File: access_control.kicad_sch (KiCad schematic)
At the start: 32 parts, among them J1 Conn_01x04_Pin, J2 Screw_Terminal_01x04, J3 Screw_Terminal_01x04, SW1 Reset button, U1 STM32F446RETx, U2 DS3231M, U3 MAX3232ESE, Y1 16MHz

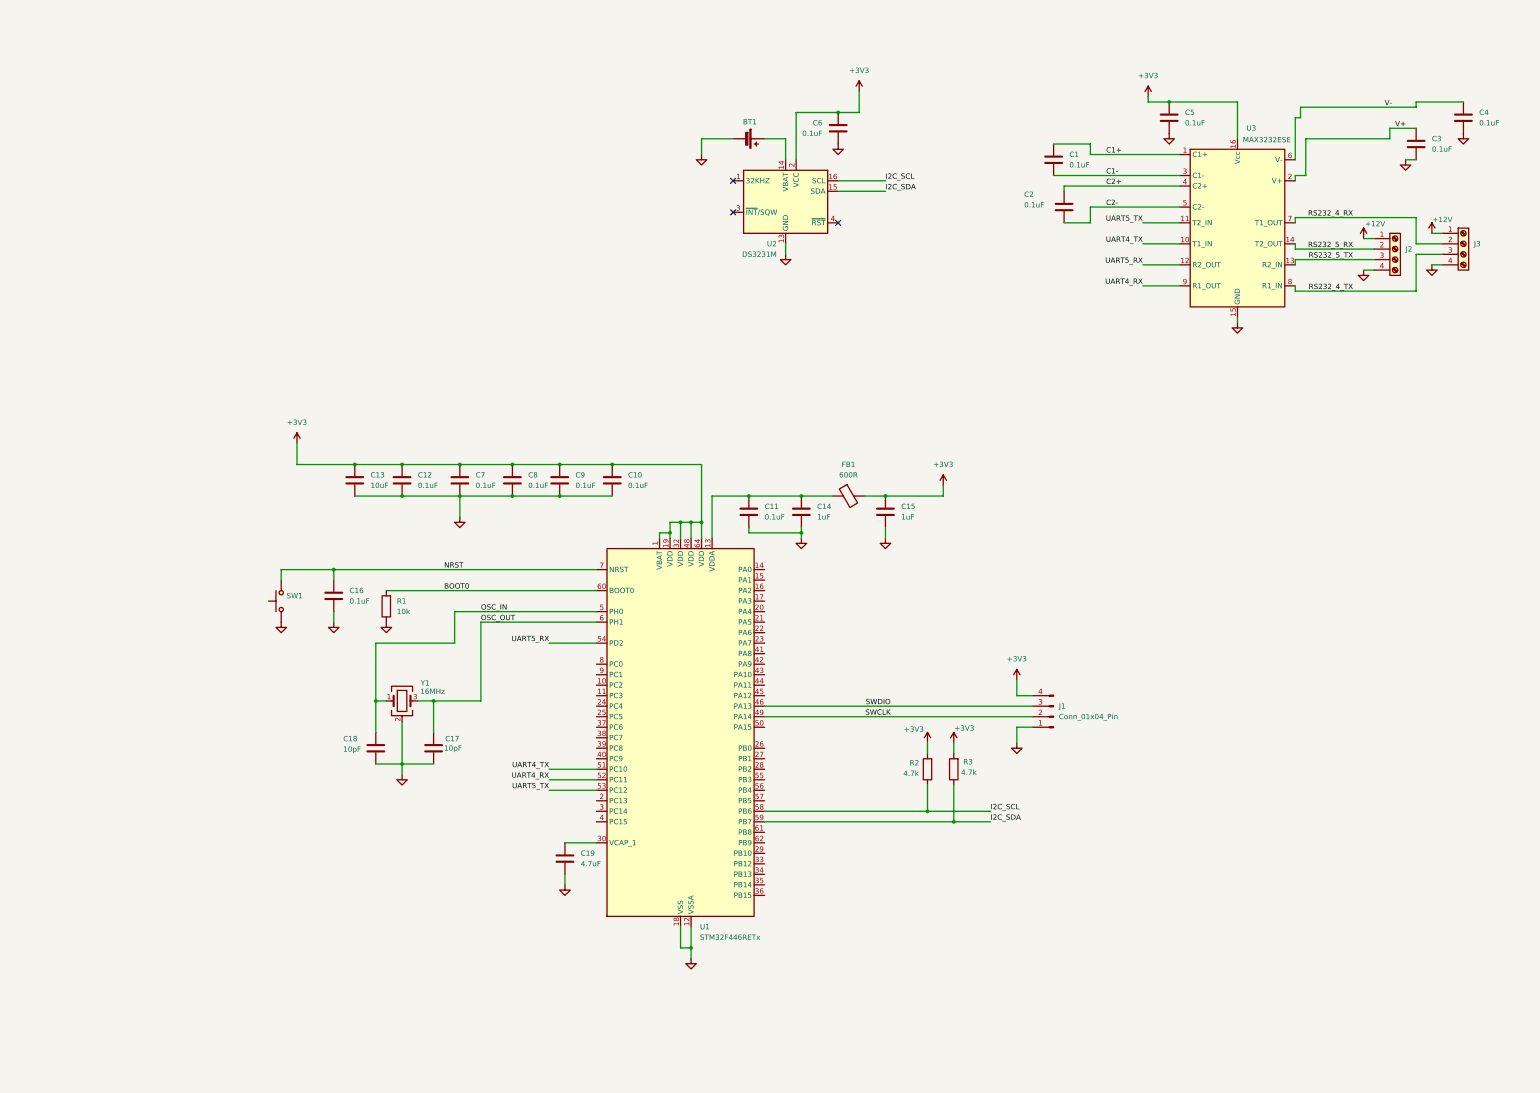
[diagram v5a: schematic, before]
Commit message: Connected the MOSFETS to the door control pins. Added footprints and info about the mosfets that i will use. Same information added for the voltage regulator
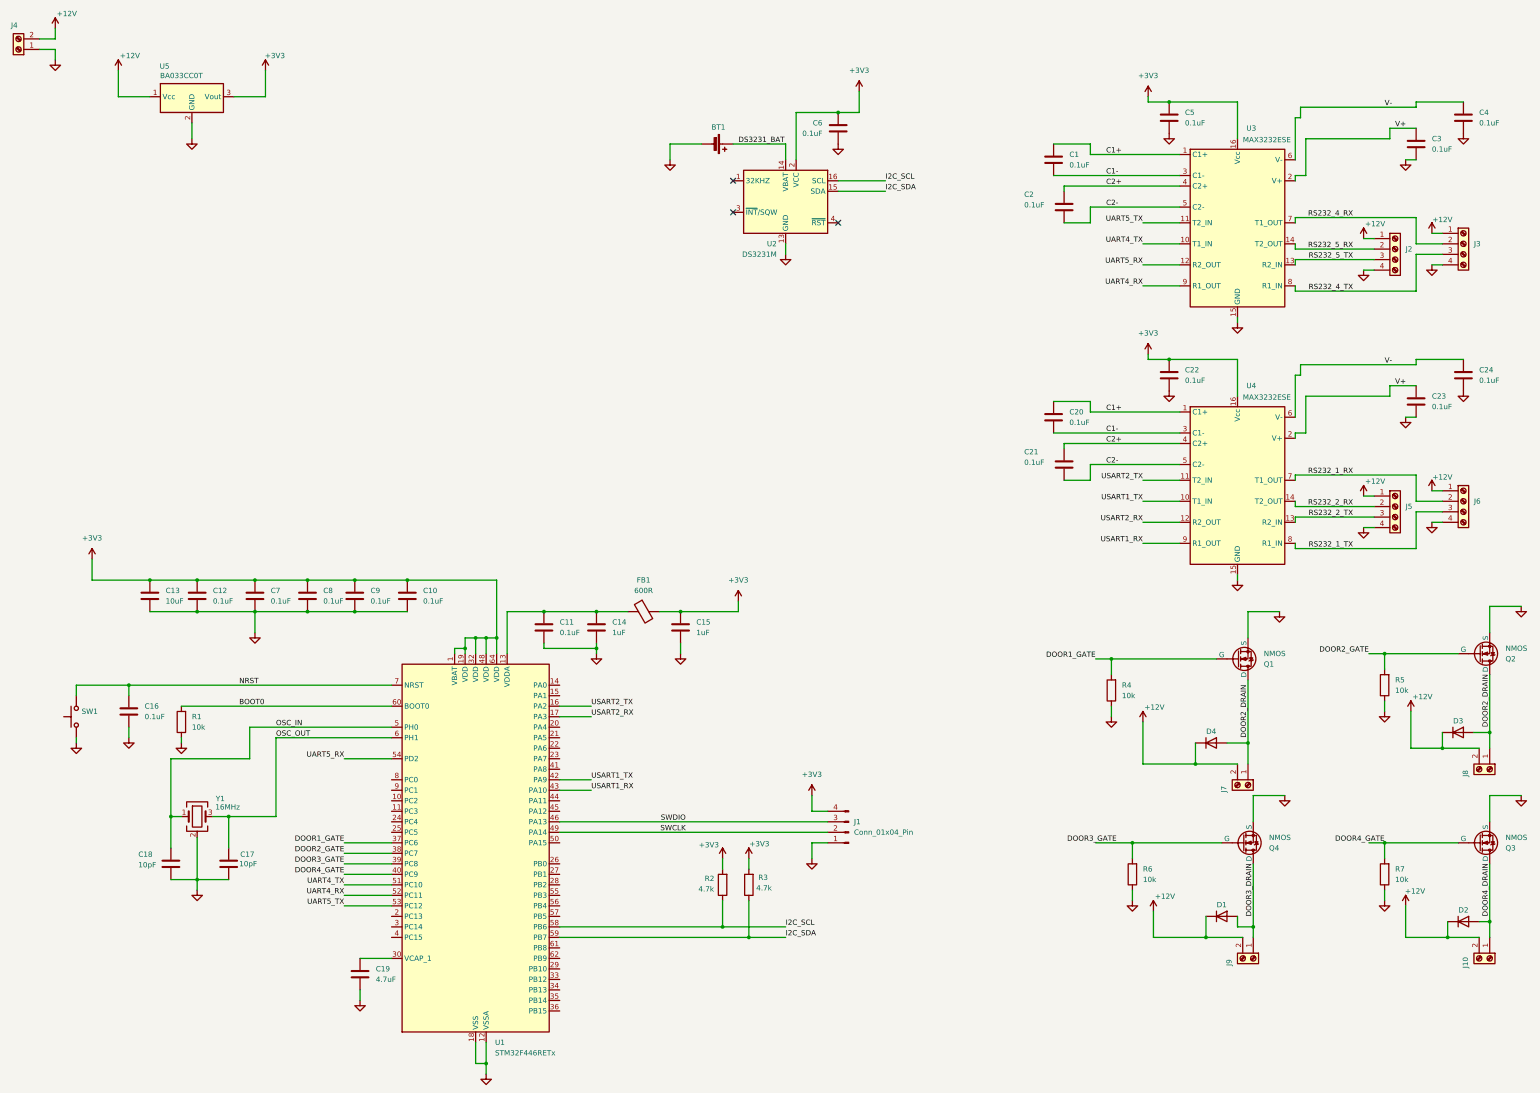
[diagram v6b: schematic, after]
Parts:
- added C20, C21, C22, C23, C24: 0.1uF, Capacitor_SMD:C_0805_2012Metric_Pad1.18x1.45mm_HandSolder, symbol Device:C
- added D1, D2, D3, D4: D, symbol Device:D
- added J10, J4, J7, J8, J9: Screw_Terminal_01x02, TerminalBlock_Phoenix:TerminalBlock_Phoenix_MKDS-1,5-2-5.08_1x02_P5.08mm_Horizontal, symbol Connector:Screw_Terminal_01x02
- added J5, J6: Screw_Terminal_01x04, TerminalBlock_Phoenix:TerminalBlock_Phoenix_MKDS-1,5-4-5.08_1x04_P5.08mm_Horizontal, symbol Connector:Screw_Terminal_01x04
- added Q1, Q2, Q3, Q4: NMOS, Package_TO_SOT_SMD:SOT-23_Handsoldering, symbol Simulation_SPICE:NMOS
- added R4, R5, R6, R7: 10k, Resistor_SMD:R_0805_2012Metric_Pad1.20x1.40mm_HandSolder, symbol Device:R
- added U4: MAX3232ESE, Package_SO:SOIC-16_3.9x9.9mm_P1.27mm, symbol max3232_symbol:MAX3232ESE
- added U5: BA033CC0T, Package_TO_SOT_THT:TO-220-3_Vertical, symbol voltage_regulator:BA033CC0T
- J2, J3: footprint (none) -> TerminalBlock_Phoenix:TerminalBlock_Phoenix_MKDS-1,5-4-5.08_1x04_P5.08mm_Horizontal
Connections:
- net +12V: now also D1.1 (K), D2.1 (K), D3.1 (K), D4.1 (K), J10.2 (Pin_2), J4.2 (Pin_2), J5.1 (Pin_1), J6.1 (Pin_1), J7.2 (Pin_2), J8.2 (Pin_2), J9.2 (Pin_2), U5.1 (Vcc)
- net +3V3: now also C22.1, U4.16 (Vcc), U5.3 (Vout)
- net C1+: now also C20.1, U4.1 (C1+)
- net C1-: now also C20.2, U4.3 (C1-)
- net C2+: now also C21.1, U4.4 (C2+)
- net C2-: now also C21.2, U4.5 (C2-)
- net GND: now also C22.2, C23.2, C24.2, J4.1 (Pin_1), J5.4 (Pin_4), J6.4 (Pin_4), Q1.3 (S), Q2.3 (S), Q3.3 (S), Q4.3 (S), R4.1, R5.1, R6.1, R7.1, U4.15 (GND), U5.2 (GND)
- net V+: now also C23.1, U4.2 (V+)
- net V-: now also C24.1, U4.6 (V-)
- net DS3231_BAT: now reaches BT1.1 (+), U2.14 (VBAT)
- net USART2_TX: now reaches U1.16 (PA2)
- net USART2_TX: now also U4.11 (T2_IN)
- net USART2_RX: now reaches U1.17 (PA3)
- net USART2_RX: now also U4.12 (R2_OUT)
- net DOOR1_GATE: now reaches U1.37 (PC6)
- net DOOR1_GATE: now also Q1.2 (G), R4.2
- net DOOR2_GATE: now reaches U1.38 (PC7)
- net DOOR2_GATE: now also Q2.2 (G), R5.2
- net DOOR3_GATE: now reaches U1.39 (PC8)
- net DOOR3_GATE: now also Q4.2 (G), R6.2
- net DOOR4_GATE: now reaches U1.40 (PC9)
- net DOOR4_GATE: now also Q3.2 (G), R7.2
- net USART1_TX: now reaches U1.42 (PA9)
- net USART1_TX: now also U4.10 (T1_IN)
- net USART1_RX: now reaches U1.43 (PA10)
- net USART1_RX: now also U4.9 (R1_OUT)
- new net DOOR2_DRAIN: D3.2 (A), D4.2 (A), J7.1 (Pin_1), J8.1 (Pin_1), Q1.1 (D), Q2.1 (D)
- new net DOOR3_DRAIN: D1.2 (A), J9.1 (Pin_1), Q4.1 (D)
- new net DOOR4_DRAIN: D2.2 (A), J10.1 (Pin_1), Q3.1 (D)
- new net RS232_1_RX: J6.2 (Pin_2), U4.7 (T1_OUT)
- new net RS232_1_TX: J6.3 (Pin_3), U4.8 (R1_IN)
- new net RS232_2_RX: J5.2 (Pin_2), U4.14 (T2_OUT)
- new net RS232_2_TX: J5.3 (Pin_3), U4.13 (R2_IN)
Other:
- moved on the sheet: BT1, C10, C11, C12, C13, C14, C15, C16, C17, C18, C19, C7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

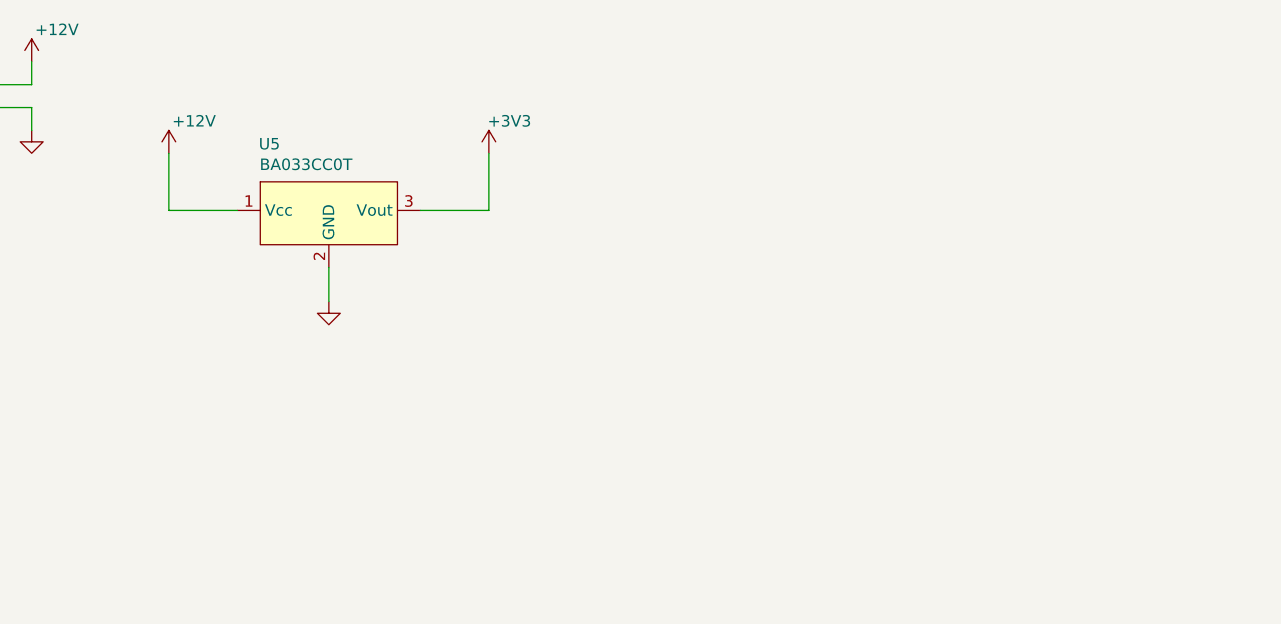
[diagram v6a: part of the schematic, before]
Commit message: Placed the needed capacitors around the BA033CC0T
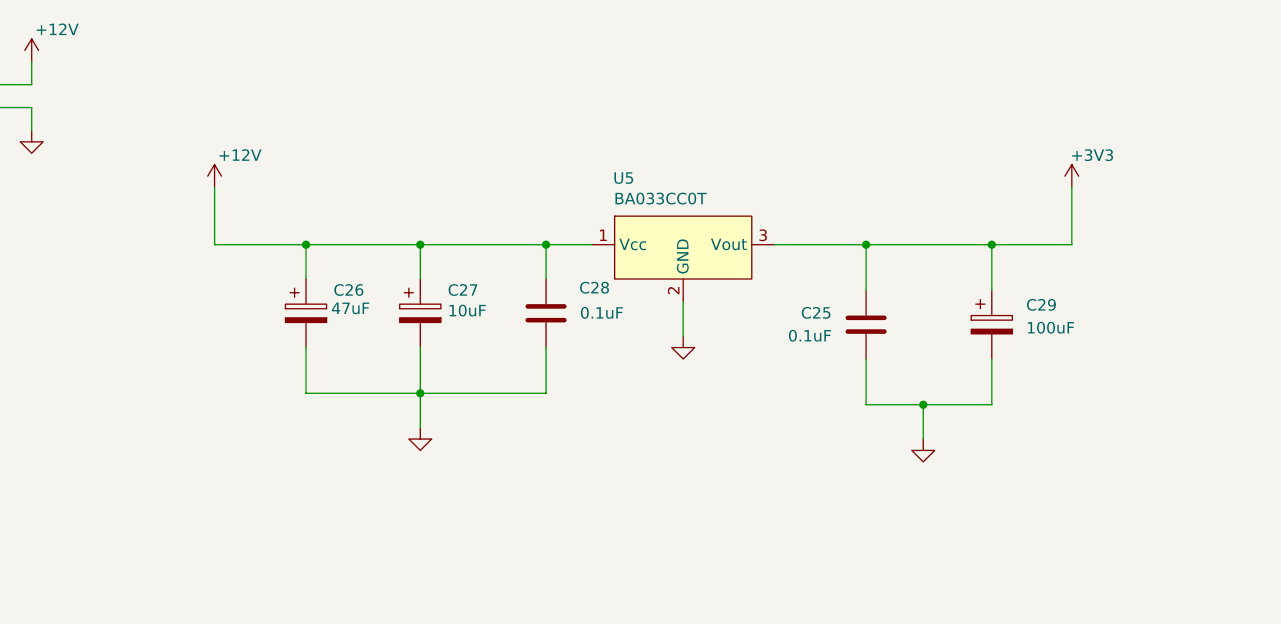
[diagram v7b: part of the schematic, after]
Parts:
- added C25, C28: 0.1uF, Capacitor_SMD:C_0805_2012Metric_Pad1.18x1.45mm_HandSolder, symbol Device:C
- added C26: 47uF, symbol Device:C_Polarized
- added C27: 10uF, symbol Device:C_Polarized
- added C29: 100uF, symbol Device:C_Polarized
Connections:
- net +12V: now also C26.1, C27.1, C28.1
- net +3V3: now also C25.1, C29.1
- net GND: now also C25.2, C26.2, C27.2, C28.2, C29.2
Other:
- moved on the sheet: U5

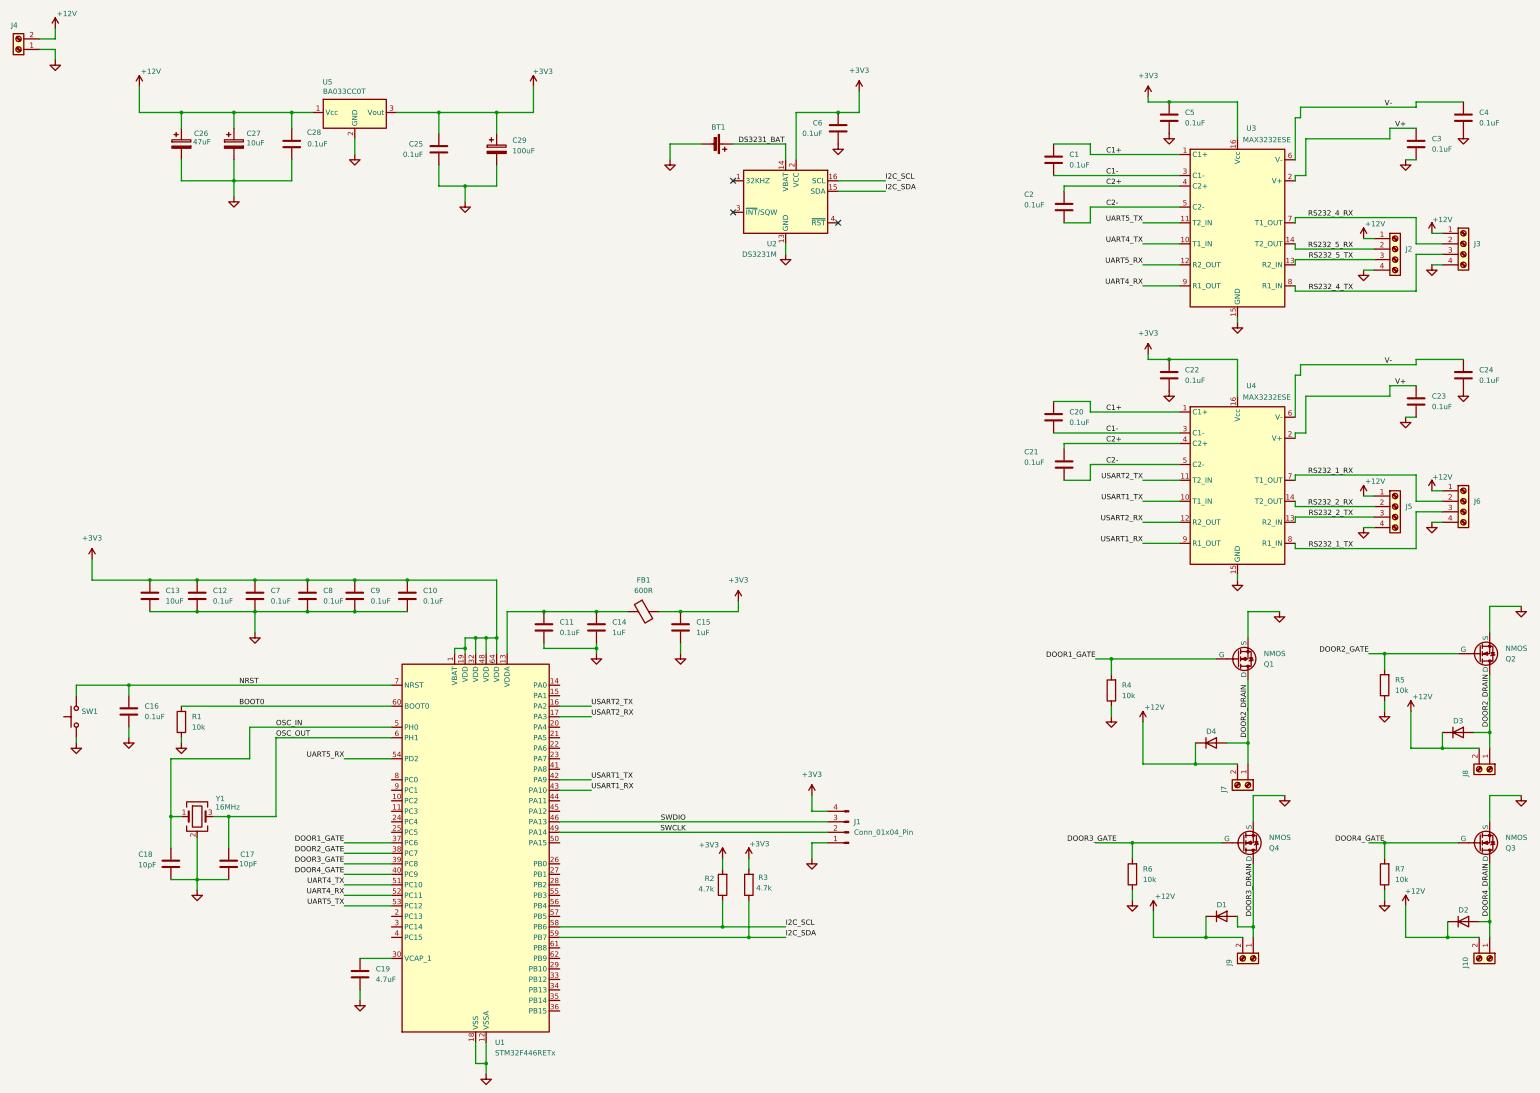
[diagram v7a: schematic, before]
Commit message: Added pull up resistor 10k to the NRST pin
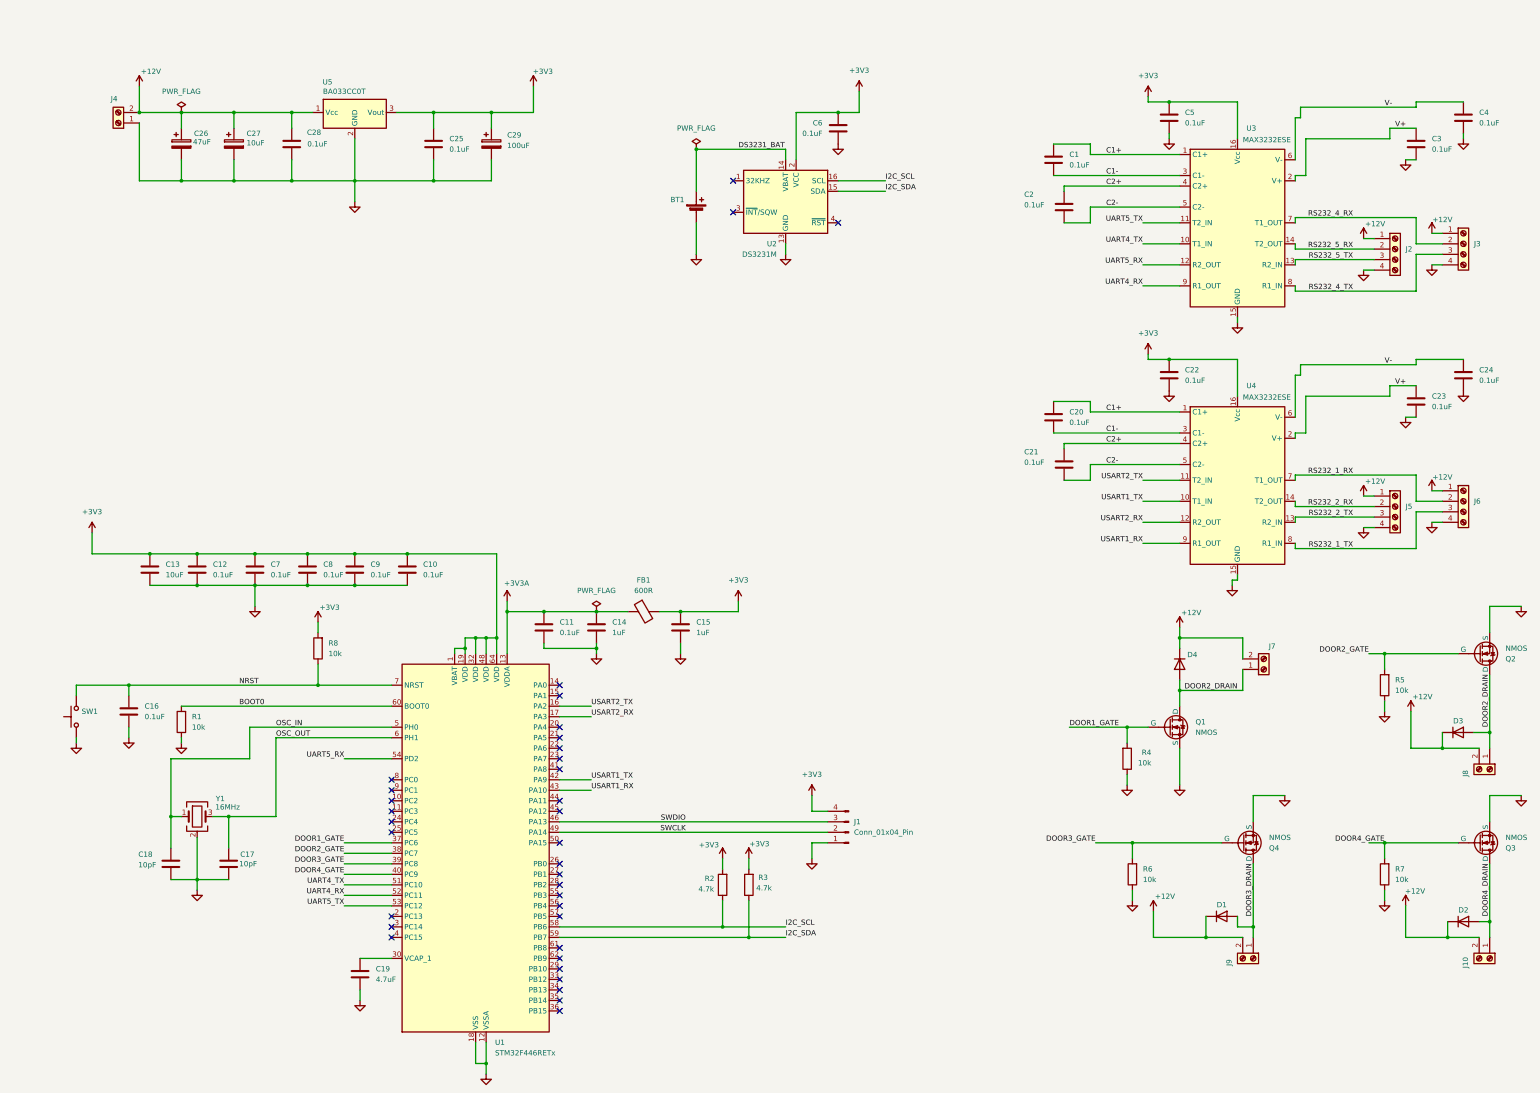
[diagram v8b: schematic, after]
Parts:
- added R8: 10k, Resistor_SMD:R_0805_2012Metric_Pad1.20x1.40mm_HandSolder, symbol Device:R
- C26: footprint (none) -> Capacitor_THT:CP_Radial_D6.3mm_P2.50mm; Distributor Link 1 (none) -> https://store.comet.bg/Catalogue/Product/37028/; MPN (none) -> EXR470M35B; Manufacturer (none) -> HITANO ENTERPRISE CORP.
- C27: footprint (none) -> Capacitor_THT:CP_Radial_D5.0mm_P2.50mm; Distributor Link 1 (none) -> https://store.comet.bg/Catalogue/Product/36186/; MPN (none) -> RK1V100M-TSD11; Manufacturer (none) -> FUJICON
- C29: footprint (none) -> Capacitor_THT:CP_Radial_D6.3mm_P2.50mm; Distributor Link 1 (none) -> https://store.comet.bg/Catalogue/Product/3826/; MPN (none) -> RM1C101M-RBE07; Manufacturer (none) -> FUJICON
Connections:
- net +3V3: now also R8.2
- net NRST: now also R8.1
- net +3V3A: now reaches C11.1, C14.1, FB1.1, U1.13 (VDDA)
- no-connect marks 3 -> 35
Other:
- moved on the sheet: BT1, C10, C12, C13, C25, C29, C7, C8, C9, D4, J4, J7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
